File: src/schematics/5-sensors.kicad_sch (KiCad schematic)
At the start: 0 parts

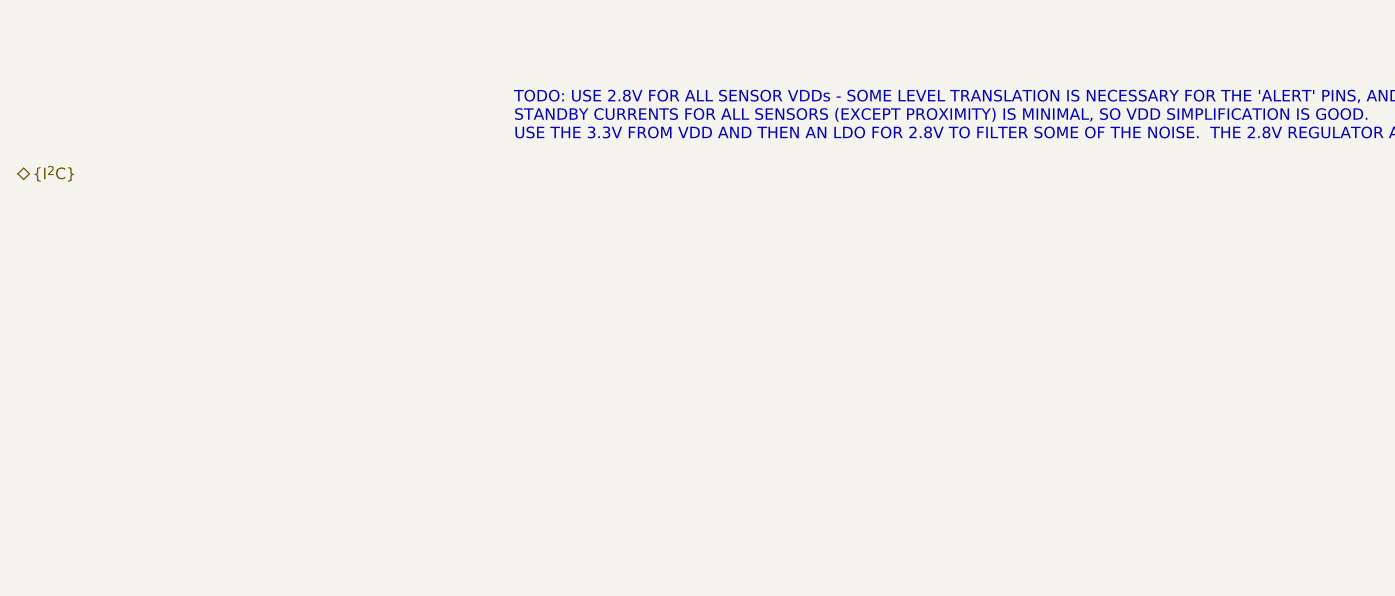
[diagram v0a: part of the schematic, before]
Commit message: Further elaboration of the design, particularly around the power budget.  It's clear that the USB Suspend current of 2.5mA won't be met, mainly due to the DPS1133 power switch's quiescent current.  This is a nice part worth keeping though as it contains OVP, OCP and reverse voltage protection all in one, up to 24V maximum input.
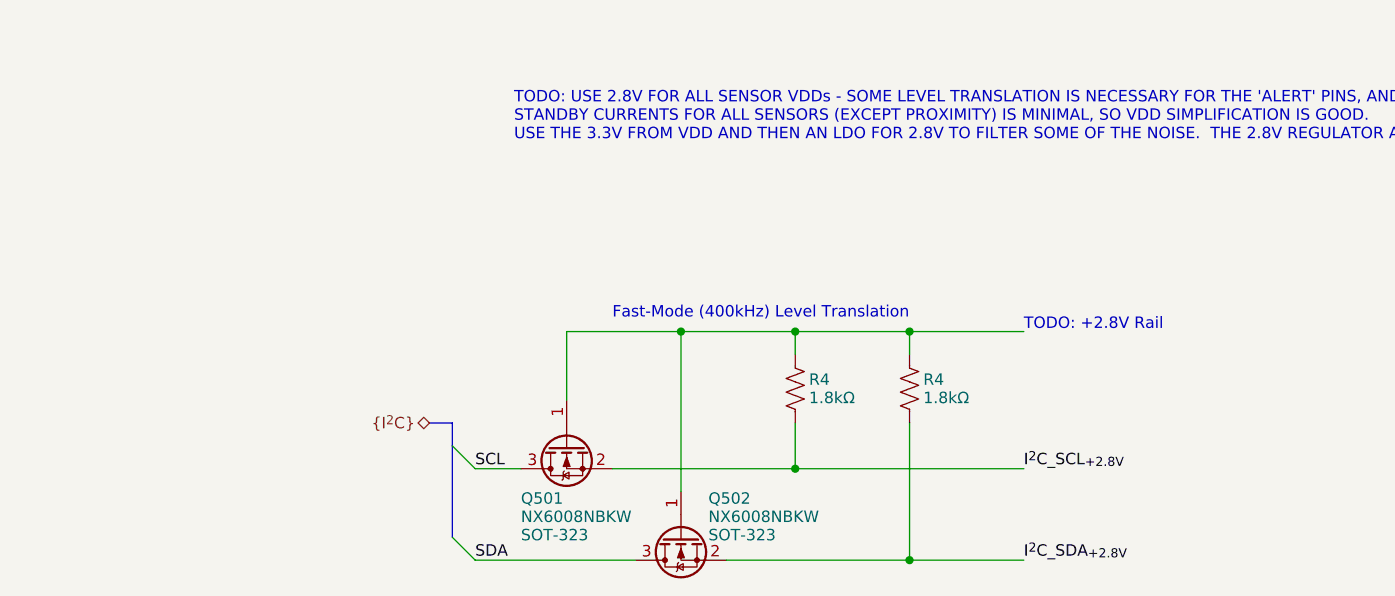
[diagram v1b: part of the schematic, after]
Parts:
- added Q501, Q502: NX6008NBKW, restall-generic-sot:SOT-323, symbol restall-manufacturer-nexperia:NX6008NBKW
- added R4 (x2): 1.8kΩ, restall-generic-resistors:nominal-0402-1005, symbol restall-generic-resistors:resistor
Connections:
- new net: Q501.1 (G), Q502.1 (G), R4.1, R4.1
- new net I^{2}C_SCL_{+2.8V}: Q501.2 (S), R4.2
- new net I^{2}C_SDA_{+2.8V}: Q502.2 (S), R4.2
- new net SCL: Q501.3 (D)
- new net SDA: Q502.3 (D)
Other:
- note added: "Fast-Mode (400kHz) Level Translation"
- note added: "TODO: +2.8V Rail"

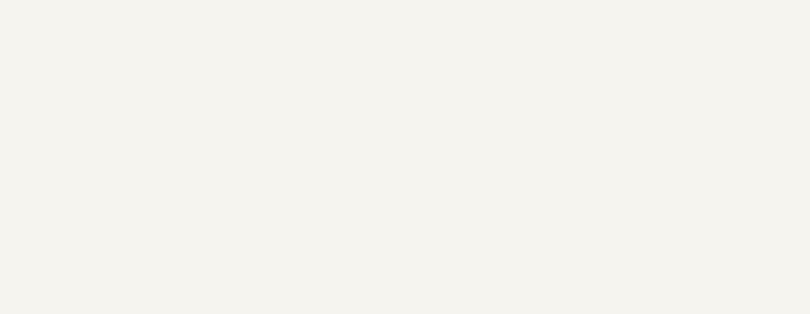
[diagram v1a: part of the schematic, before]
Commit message: Elaboration of the top-level schematicd.
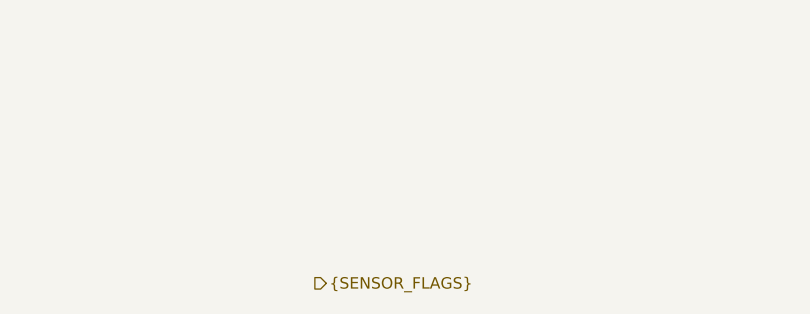
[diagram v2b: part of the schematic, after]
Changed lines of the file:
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@@
     (effects (font (size 1.27 1.27)) (justify left bottom))
   )
-  (label "SDA" (at 127 144.78 0)
+  (label "SDA" (at 127 144.78 0) (fields_autoplaced)
     (effects (font (size 1.27 1.27)) (justify left bottom))
   )
@@
     (effects (font (size 1.27 1.27)) (justify left bottom))
   )
-  (label "SCL" (at 127 134.62 0)
+  (label "SCL" (at 127 134.62 0) (fields_autoplaced)
     (effects (font (size 1.27 1.27)) (justify left bottom))
   )
@@
     (effects (font (size 1.27 1.27)) (justify left bottom))
   )
+  (hierarchical_label "{SENSOR_FLAGS}" (shape output) (at 279.146 152.146 0) (fields_autoplaced)
+    (effects (font (size 1.27 1.27)) (justify left))
+  )
   (hierarchical_label "{I^{2}C}" (shape bidirectional) (at 121.92 129.54 180) (fields_autoplaced)

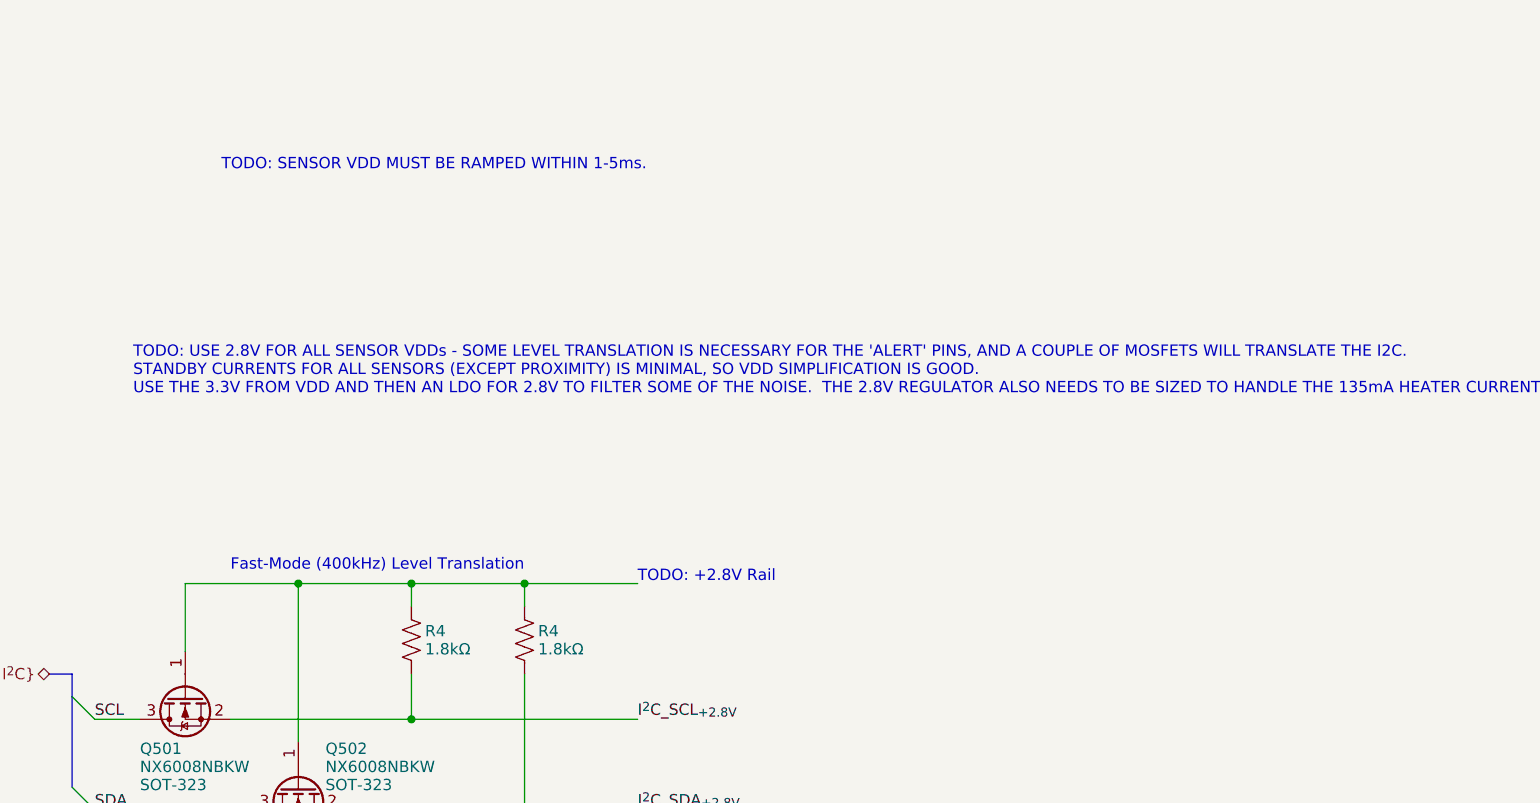
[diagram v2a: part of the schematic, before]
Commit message: Further elaboration of the design and schematics, mainly power supply calculations.
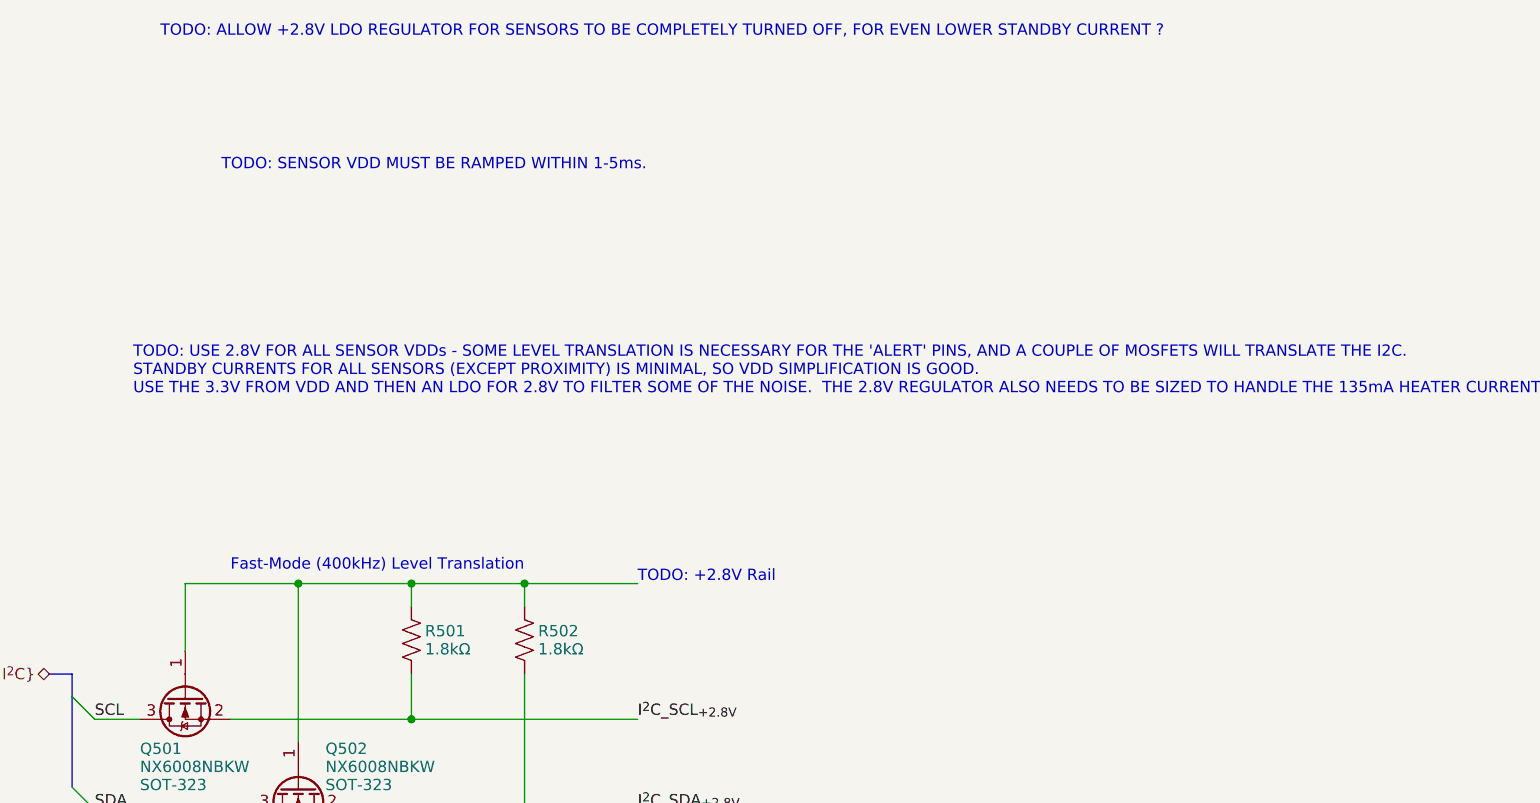
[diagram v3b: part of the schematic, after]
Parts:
- renumbered R4 to R501, R4 to R502
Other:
- note added: "TODO: ALLOW +2.8V LDO REGULATOR FOR SENSORS TO BE COMPLETELY TURNED OFF, FOR EVEN LOWER STANDBY CURRENT ?"
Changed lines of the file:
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@@
+    (effects (font (size 1.27 1.27)) (justify left bottom))
+  )
+  (text "TODO: ALLOW +2.8V LDO REGULATOR FOR SENSORS TO BE COMPLETELY TURNED OFF, FOR EVEN LOWER STANDBY CURRENT ?"
+    (at 134.366 58.166 0)
     (effects (font (size 1.27 1.27)) (justify left bottom))
   )
@@
   (symbol (lib_id "restall-generic-resistors:resistor") (at 162.56 125.73 0) (unit 1)
     (in_bom yes) (on_board yes) (dnp no)
-    (property "Reference" "R4" (at 164.084 124.714 0)
+    (property "Reference" "R501" (at 164.084 124.714 0)
       (effects (font (size 1.27 1.27)) (justify left))
     )
@@
     (instances
       (project "msf-owl-clock"
-        (path "/56d623d3-22db-4d43-a9d9-e6bb4bb68946/cc278a5b-e802-444a-81ef-f38d11985404"
-          (reference "R4") (unit 1)
-        )
-        (path "/56d623d3-22db-4d43-a9d9-e6bb4bb68946"
-          (reference "R001") (unit 1)
-        )
         (path "/56d623d3-22db-4d43-a9d9-e6bb4bb68946/f496ae57-4ed4-47d4-8c97-f77f6741aea7"
           (reference "R501") (unit 1)
@@
   (symbol (lib_id "restall-generic-resistors:resistor") (at 175.26 125.73 0) (unit 1)
     (in_bom yes) (on_board yes) (dnp no)
-    (property "Reference" "R4" (at 176.784 124.714 0)
+    (property "Reference" "R502" (at 176.784 124.714 0)
       (effects (font (size 1.27 1.27)) (justify left))
     )
@@
     (instances
       (project "msf-owl-clock"
-        (path "/56d623d3-22db-4d43-a9d9-e6bb4bb68946/cc278a5b-e802-444a-81ef-f38d11985404"
-          (reference "R4") (unit 1)
-        )
-        (path "/56d623d3-22db-4d43-a9d9-e6bb4bb68946"
-          (reference "R001") (unit 1)
-        )
         (path "/56d623d3-22db-4d43-a9d9-e6bb4bb68946/f496ae57-4ed4-47d4-8c97-f77f6741aea7"
           (reference "R502") (unit 1)

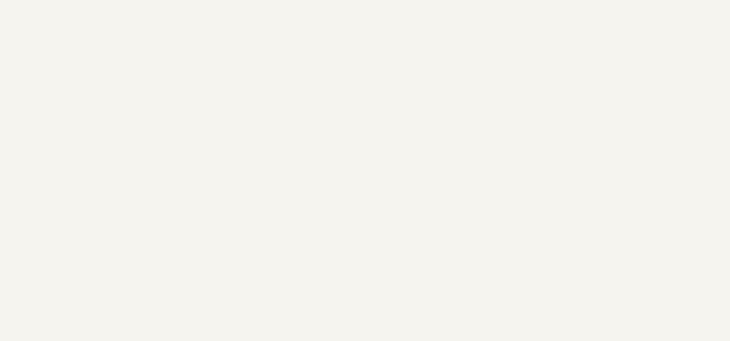
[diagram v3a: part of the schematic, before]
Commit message: Started to draw the MSF receiver based on the simulation learnings.
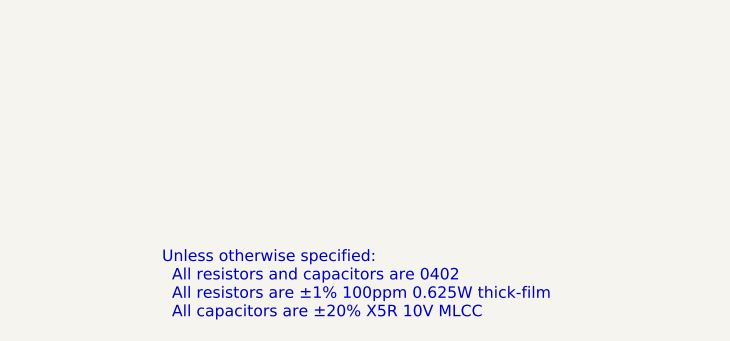
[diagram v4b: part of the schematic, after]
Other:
- note added: "Unless otherwise specified: All resistors and capacitors are 0402 All resistors are ±1% 100ppm 0.625W thick-film All capacitors are ±20% X5R 10V MLCC"
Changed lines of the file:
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@@
+    (effects (font (size 1.27 1.27)) (justify left bottom))
+  )
+  (text "Unless otherwise specified:\n  All resistors and capacitors are 0402\n  All resistors are ±1% 100ppm 0.625W thick-film\n  All capacitors are ±20% X5R 10V MLCC "
+    (at 301.244 261.62 0)
     (effects (font (size 1.27 1.27)) (justify left bottom))
   )

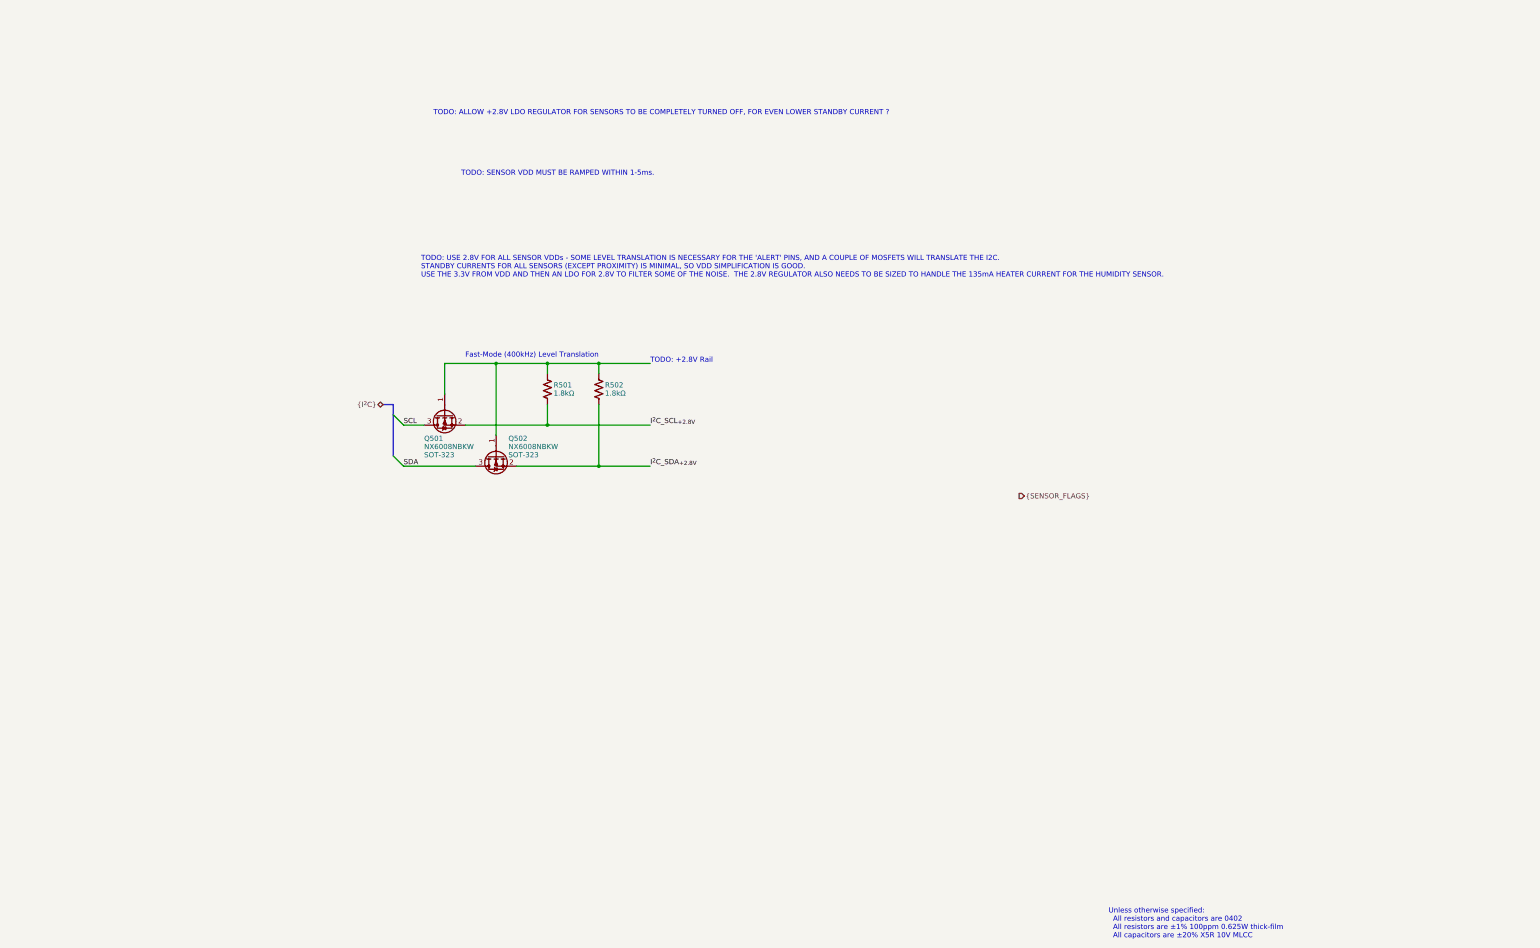
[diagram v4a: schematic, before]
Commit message: Started to draw up the sensor schematics.
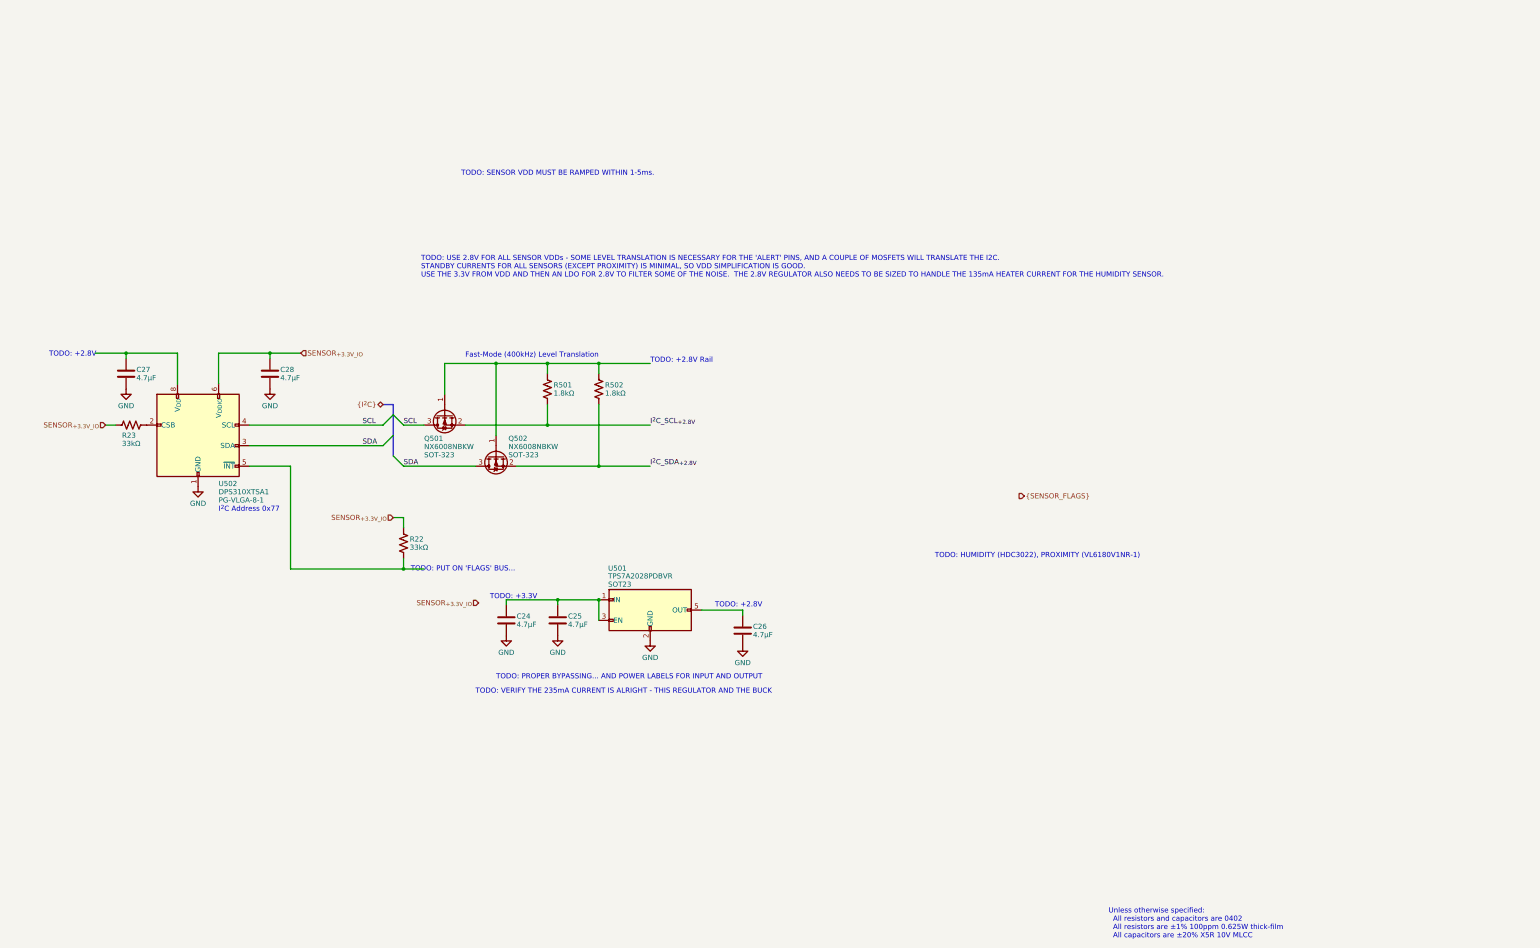
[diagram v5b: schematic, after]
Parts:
- added C24, C25, C26, C27, C28: 4.7μF, restall-generic-capacitors:unpolarised-nominal-0402-1005, symbol restall-generic-capacitors:capacitor-unpolarised
- added R22, R23: 33kΩ, restall-generic-resistors:nominal-0402-1005, symbol restall-generic-resistors:resistor
- added U501: TPS7A2028PDBVR, restall-manufacturer-ti:TPS7A20??PDBVR, symbol restall-manufacturer-ti:TPS7A20??PDBVR
- added U502: DPS310XTSA1, restall-manufacturer-infineon:PG-VLGA-8-1-2.0x2.5mm-0.65mm, symbol restall-manufacturer-infineon:DPS310XTSA1
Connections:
- net SCL: now also U502.4 (SCK)
- net SDA: now also U502.3 (SDI)
- new net: C24.1, C25.1, U501.1 (IN), U501.3 (EN)
- new net: C26.1, U501.5 (OUT)
- new net: C27.1, U502.8 (V_{DD})
- new net: R22.2, U502.5 (SDO)
- new net: R23.2, U502.2 (CSB)
- new net GND: C24.2, C25.2, C26.2, C27.2, C28.2, U501.2 (GND), U502.1 (GND), U502.7 (GND)
- new net SENSOR_{+3.3V_IO}: C28.1, R22.1, R23.1, U502.6 (V_{DDIO})
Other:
- note added: "I^{2}C Address 0x77"
- note added: "TODO: +2.8V"
- note added: "TODO: +3.3V"
- note added: "TODO: HUMIDITY (HDC3022), PROXIMITY (VL6180V1NR-1)"
- note added: "TODO: PROPER BYPASSING... AND POWER LABELS FOR INPUT AND OUTPUT"
- note added: "TODO: PUT ON 'FLAGS' BUS..."
- note added: "TODO: VERIFY THE 235mA CURRENT IS ALRIGHT - THIS REGULATOR AND THE BUCK"
- note removed: "TODO: ALLOW +2.8V LDO REGULATOR FOR SENSORS TO BE COMPLETELY TURNED OFF, FOR EVEN LOWER STANDBY CURRENT ?"
